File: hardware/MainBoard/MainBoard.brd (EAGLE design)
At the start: 90 x 56 mm, 265 parts, among them J1 CON-71741-2184-BOT, J2 CON-71741-2184-TOP, J3 CON-FTSH-105-01-L-DV-K, J4 CON-ZX62R-B-5P, J7 CON-RJ45-J0G-0007NL, J8 SWITCH-CJS-1200-1200, M1 MOUNT-HOLE3.3, M2 MOUNT-HOLE3.3, M3 MOUNT-HOLE3.3, M4 MOUNT-HOLE3.3, M5 FIDUCIAL1X2, M6 FIDUCIAL1X2, M7 FIDUCIAL1X2, M8 FIDUCIAL1X2, Q1 MMBT3904, SW1 SWITCH-ESWITCH-TL3340G, SW2 SWITCH-ESWITCH-TL3340G, U1 A2F500M3G-1FGG256, U2 MAX19706-T4877-4, U3 MAX19706-T4877-4, U4 USBLC6-2SC6, U5 FT232HL, U6 DP83848C-VBH48A, U7 93LC56BT-OT, U8 DS1818-10-SOT-23, X1 ECX-2236-200, X2 ECX-31B, X3 ASEM1-C, X5 ECX-42-120

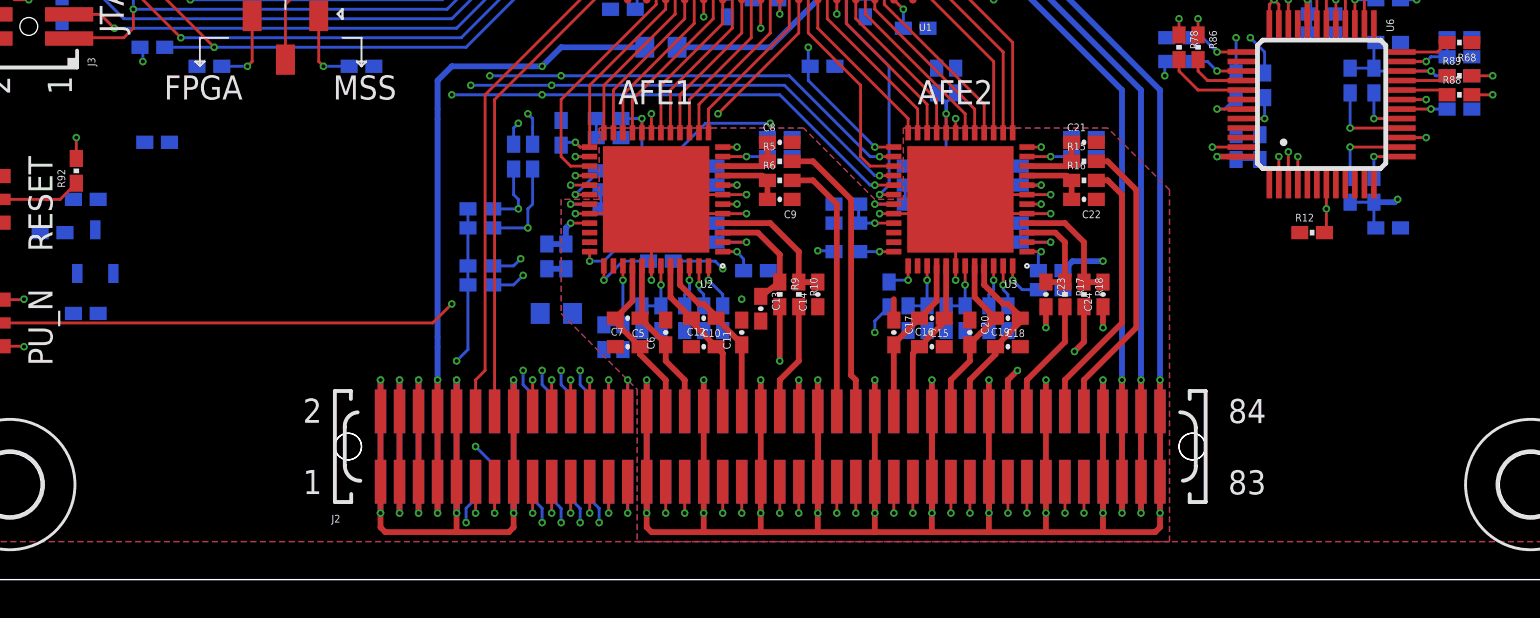
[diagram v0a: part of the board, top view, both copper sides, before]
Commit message: Moved logos to silkscreen and updated library accordingly.
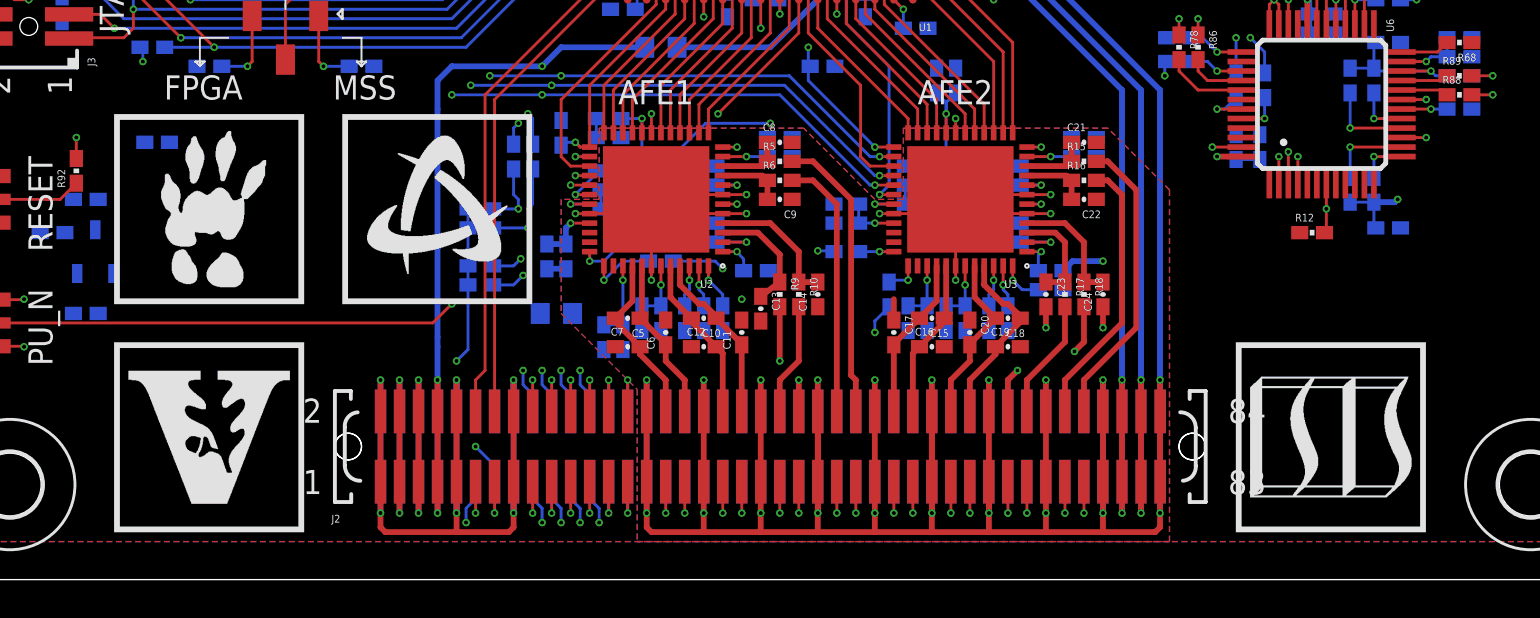
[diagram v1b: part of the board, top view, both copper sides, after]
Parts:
- LOGO1: value LOGO-ISIS-600MIL-10MM-PH -> LOGO-ISIS-600MIL-10MM-SS; device Logo:LOGO-ISIS-10MM-GOLD -> Logo:LOGO-ISIS-10MM-SILKSCREEN
- LOGO2: value LOGO-VANDERBILT-600MIL-10MM-AU -> LOGO-VANDERBILT-600MIL-10MM-SS; device Logo:LOGO-VANDERBILT-10MM-GOLD -> Logo:LOGO-VANDERBILT-10MM-SILKSCREEN
- LOGO3: value LOGO-MARMOTE-600MIL-10MM-AU -> LOGO-MARMOTE-600MIL-10MM-SS; device Logo:LOGO-MARMOTE-10MM-GOLD -> Logo:LOGO-MARMOTE-10MM-SILKSCREEN
- LOGO4: value LOGO-SMARTFUSION-600MIL-10MM-AU -> LOGO-SMARTFUSION-600MIL-10MM-SS; device Logo:LOGO-SMARTFUSION-10MM-GOLD -> Logo:LOGO-SMARTFUSION-10MM-SILKSCREEN
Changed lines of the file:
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@@
 <grid distance="1" unitdist="mm" unit="mm" style="lines" multiple="1" display="yes" altdistance="0.25" altunitdist="mm" altunit="mm"/>
 <layers>
-<layer number="1" name="Top" color="4" fill="1" visible="yes" active="yes"/>
+<layer number="1" name="Top" color="4" fill="1" visible="no" active="yes"/>
 <layer number="2" name="GND" color="1" fill="3" visible="no" active="yes"/>
-<layer number="3" name="Inner1" color="13" fill="3" visible="yes" active="yes"/>
+<layer number="3" name="Inner1" color="13" fill="3" visible="no" active="yes"/>
 <layer number="14" name="Inner2" color="10" fill="6" visible="yes" active="yes"/>
 <layer number="15" name="D3V3" color="4" fill="6" visible="no" active="yes"/>
@@
 <layer number="27" name="tValues" color="7" fill="1" visible="no" active="yes"/>
 <layer number="28" name="bValues" color="7" fill="1" visible="no" active="yes"/>
-<layer number="29" name="tStop" color="7" fill="3" visible="yes" active="yes"/>
+<layer number="29" name="tStop" color="7" fill="3" visible="no" active="yes"/>
 <layer number="30" name="bStop" color="7" fill="6" visible="no" active="yes"/>
 <layer number="31" name="tCream" color="7" fill="4" visible="no" active="yes"/>
@@
 <layer number="98" name="Guide" color="6" fill="1" visible="no" active="no"/>
 <layer number="100" name="Muster" color="7" fill="1" visible="no" active="no"/>
-<layer number="101" name="Patch_Top" color="12" fill="4" visible="no" active="yes"/>
+<layer number="101" name="Patch_Top" color="12" fill="4" visible="yes" active="yes"/>
 <layer number="102" name="Vscore" color="7" fill="1" visible="no" active="yes"/>
 <layer number="103" name="tMap" color="7" fill="1" visible="no" active="yes"/>
@@
 <rectangle x1="68" y1="4" x2="71" y2="10" layer="101"/>
 <rectangle x1="4" y1="12" x2="13" y2="23" layer="116"/>
+<rectangle x1="12" y1="25" x2="27" y2="28" layer="101"/>
 </plain>
 <attributes>
@@
 </autorouter>
 <elements>
-<element name="LOGO1" library="Logo" package="LOGO-ISIS-10MM-GOLD" value="LOGO-ISIS-600MIL-10MM-PH" x="69.5" y="2.5"/>
-<element name="LOGO2" library="Logo" package="LOGO-VANDERBILT-10MM-GOLD" value="LOGO-VANDERBILT-600MIL-10MM-AU" x="10.5" y="2.5"/>
-<element name="LOGO3" library="Logo" package="LOGO-MARMOTE-10MM-GOLD" value="LOGO-MARMOTE-600MIL-10MM-AU" x="10.5" y="14.5"/>
-<element name="LOGO4" library="Logo" package="LOGO-SMARTFUSION-10MM-GOLD" value="LOGO-SMARTFUSION-600MIL-10MM-AU" x="22.5" y="14.5"/>
+<element name="LOGO1" library="Logo" package="LOGO-ISIS-10MM-SILKSCREEN" value="LOGO-ISIS-600MIL-10MM-SS" x="69.5" y="2.5"/>
+<element name="LOGO2" library="Logo" package="LOGO-VANDERBILT-10MM-SILKSCREEN" value="LOGO-VANDERBILT-600MIL-10MM-SS" x="10.5" y="2.5"/>
+<element name="LOGO3" library="Logo" package="LOGO-MARMOTE-10MM-SILKSCREEN" value="LOGO-MARMOTE-600MIL-10MM-SS" x="10.5" y="14.5"/>
+<element name="LOGO4" library="Logo" package="LOGO-SMARTFUSION-10MM-SILKSCREEN" value="LOGO-SMARTFUSION-600MIL-10MM-SS" x="22.5" y="14.5"/>
 <element name="U1" library="MainBoard" package="FG256" value="A2F500M3G-1FGG256" x="45" y="38" rot="R180">
 <attribute name="DIGI-KEY#" value="1100-1007-ND" x="45" y="38" size="1.778" layer="27" rot="R180" display="off"/>
@@
 </signal>
 </signals>
-<errors>
-</errors>
 </board>
 </drawing>

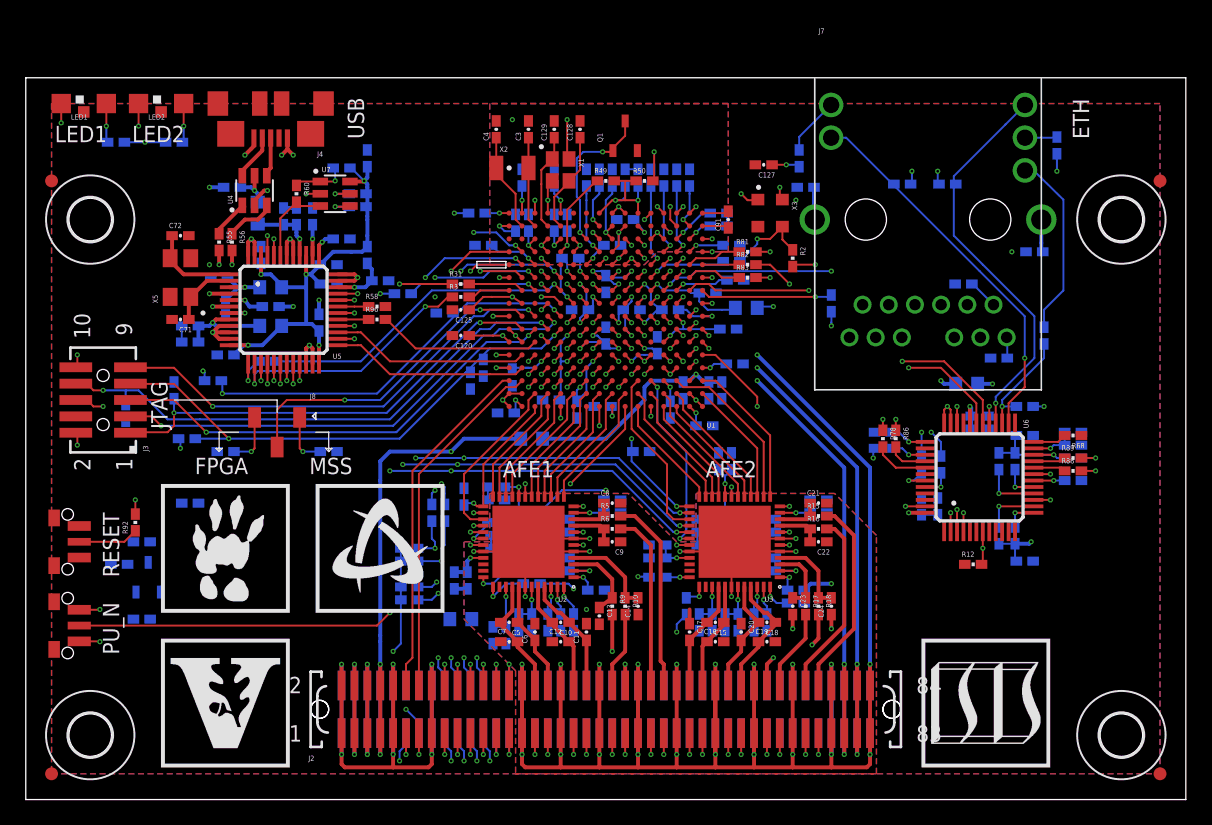
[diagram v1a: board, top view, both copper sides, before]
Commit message: Revised signal angles.
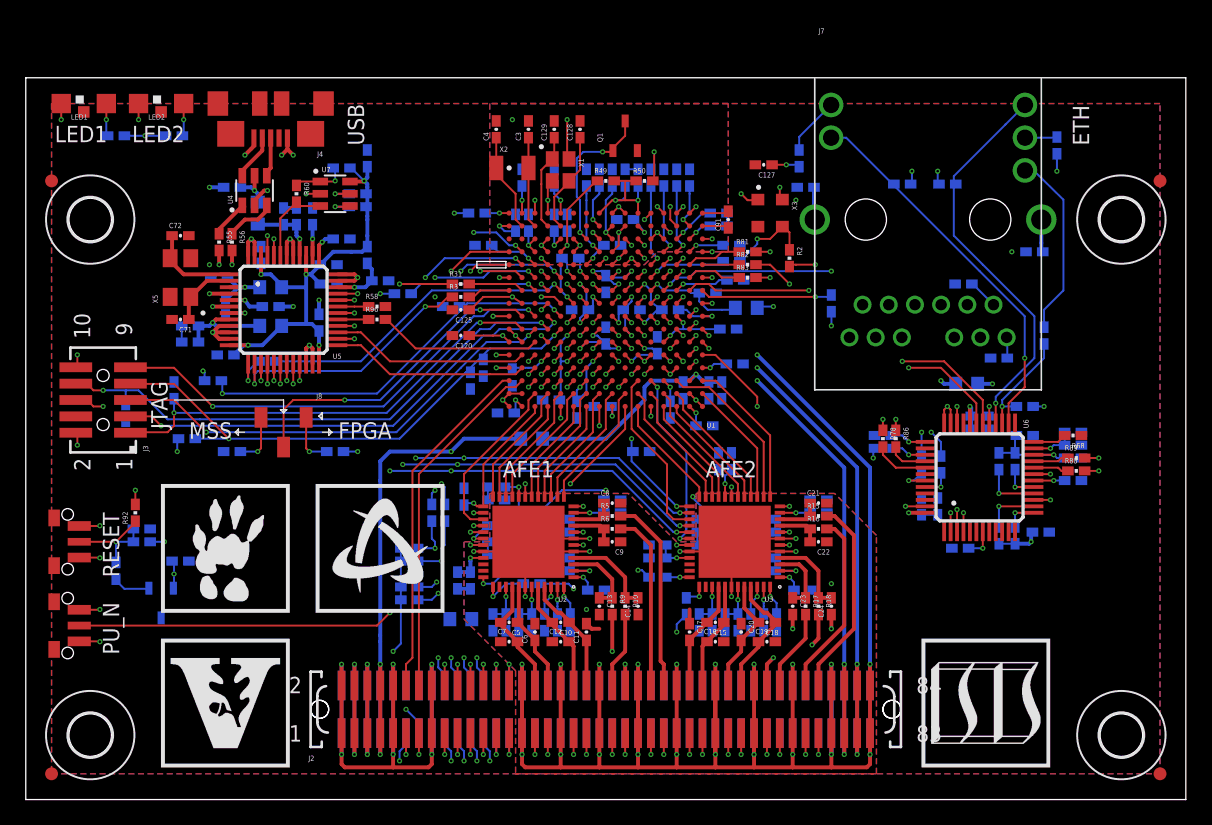
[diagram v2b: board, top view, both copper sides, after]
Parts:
- moved R91 6.00 mm to (9.00, 20.0)
- moved C130 4.56 mm to (12.0, 18.5)
- moved C80 2.57 mm to (78.8, 20.8)
- moved U8 2.24 mm to (10.5, 15.2), turned to 270 degrees
- moved C62 2.12 mm to (58.2, 13.8), turned to 270 degrees
- moved R12 1.60 mm to (72.5, 19.5), flipped to the bottom, turned to 180 degrees
- moved C36 1.00 mm to (36.2, 13.8)
- moved C37 1.00 mm to (37.2, 13.8)
- moved C90 1.00 mm to (9.00, 21.0)
- moved C13 0.75 mm to (44.5, 15.0)
- moved R92 0.75 mm to (8.50, 22.2)
- moved C74 0.71 mm to (33.0, 38.2)
- moved C32 0.56 mm to (36.5, 20.0)
- moved C33 0.56 mm to (36.5, 19.0)
- moved R93 0.56 mm to (7.00, 17.8), turned to 90 degrees
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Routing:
- net !MSS_RESET_PB: track 4.95 -> 9.02 mm, vias 0 -> 1
- net D3V3: track 129.1 -> 132.7 mm, vias 44 -> 48
- net EXTIC-RST: track 0.00 -> 2.94 mm
- net DGND: track 145.1 -> 147.5 mm, vias 75 -> 77
- net AGND: track 266.8 -> 264.7 mm
- net A3V3: track 127.6 -> 126.5 mm
- net VJTAG: track 42.9 -> 43.8 mm
- net E3V3: track 51.6 -> 50.9 mm
- net LED2H: track 3.03 -> 2.53 mm
- net LED1H: track 3.03 -> 2.53 mm
- net JTAGSEL: track 25.3 -> 24.8 mm

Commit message: Checked GND and PWR vias.
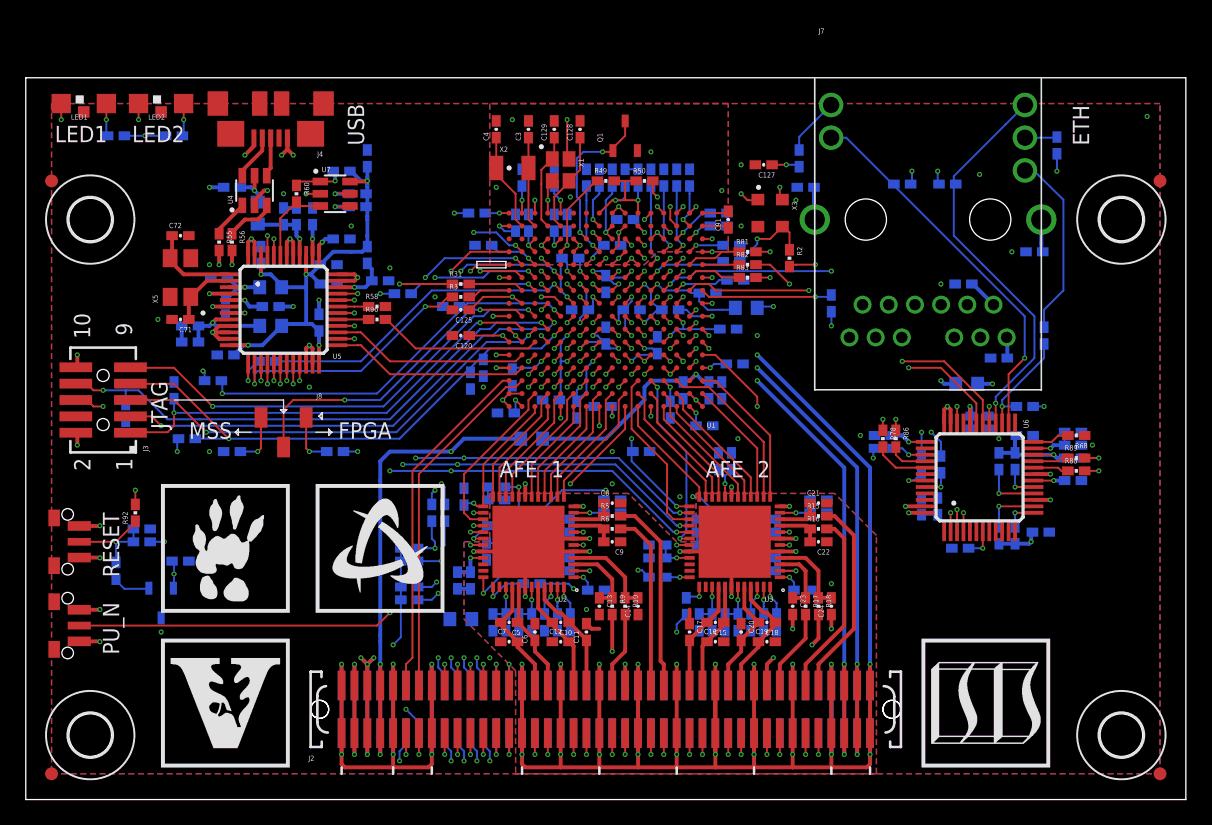
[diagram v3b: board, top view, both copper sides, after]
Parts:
- moved C32 0.79 mm to (36.8, 19.2), turned to 270 degrees
- moved C33 0.79 mm to (35.8, 19.2), turned to 270 degrees
- moved R61 0.25 mm to (24.5, 48.8)
- moved R68 0.25 mm to (81.5, 28.2)
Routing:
- net D3V3: track 132.7 -> 135.3 mm, vias 48 -> 50
- net A3V3: track 126.5 -> 125.0 mm
- net AUX_DAC2: track 5.74 -> 6.80 mm
- net AGND: track 264.7 -> 264.3 mm, vias 50 -> 54
- net DGND: vias 77 -> 99
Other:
- board text added: "1"
- board text added: "2"
- board text added: "AFE"
- board text removed: "AFE1"
- board text removed: "AFE2"

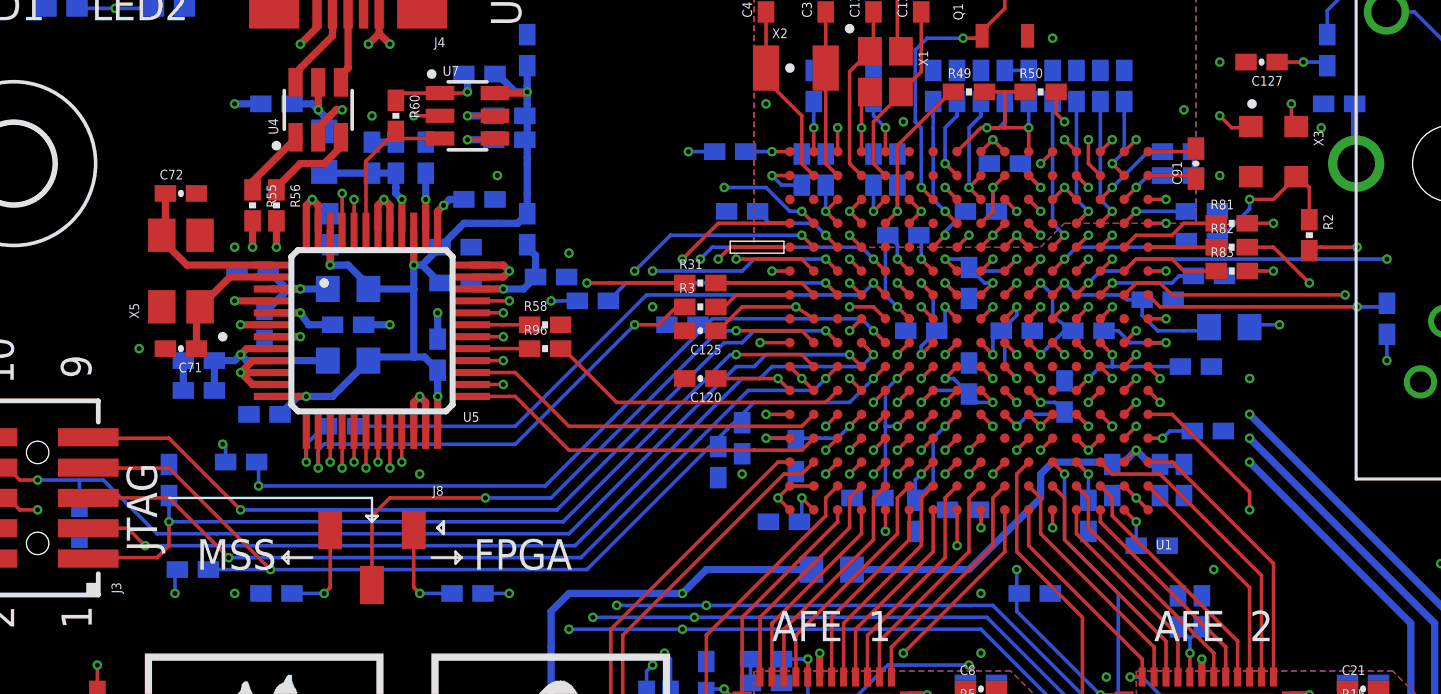
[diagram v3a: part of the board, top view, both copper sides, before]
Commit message: Added test vias.
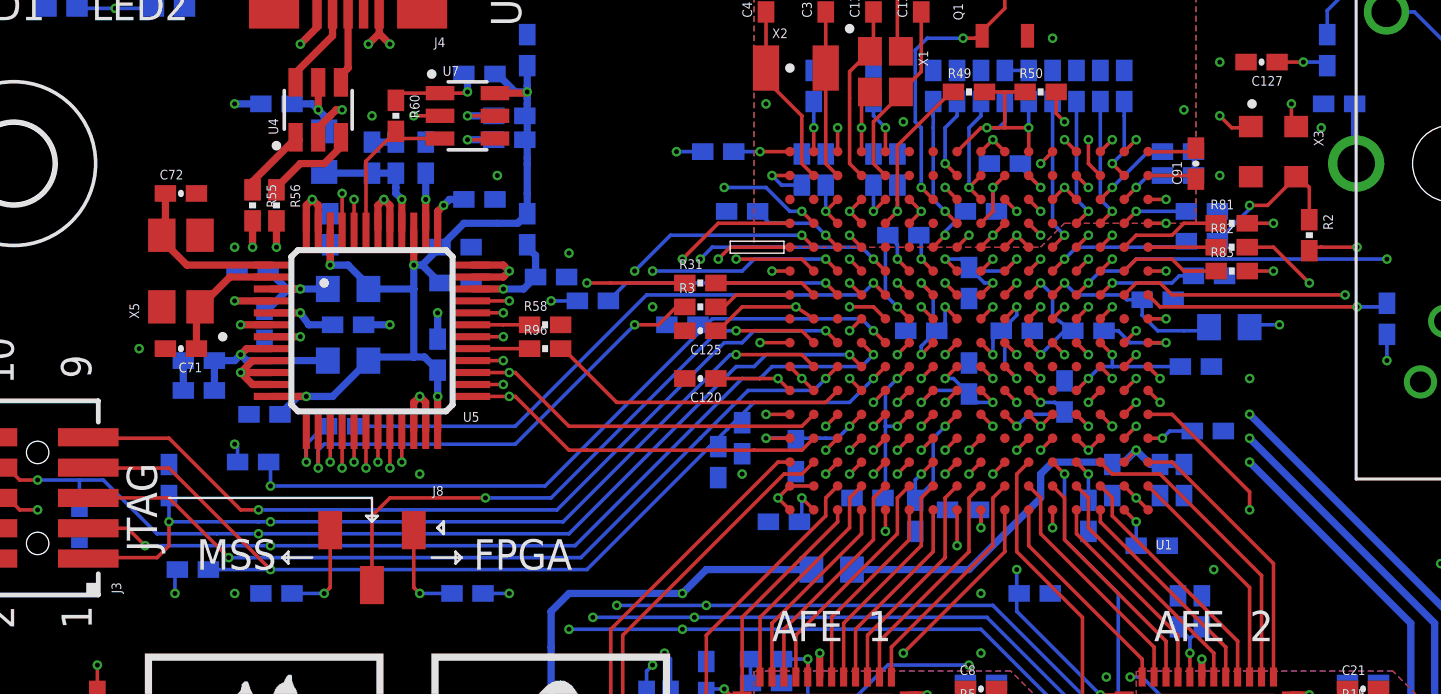
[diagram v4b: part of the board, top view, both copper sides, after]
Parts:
- moved R8 0.50 mm to (15.0, 32.5)
- moved R94 0.50 mm to (34.5, 45.5)
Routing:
- net TRST: vias 2 -> 3
- net TDO: vias 2 -> 3
- net TCK: vias 2 -> 3
- net !WR: vias 0 -> 1
- net !TXE: vias 0 -> 1
